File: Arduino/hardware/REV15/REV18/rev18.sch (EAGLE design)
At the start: 3 parts

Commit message: up to rev18 cleaned up
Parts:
- added IC1: DS1820, DS1820:DS1820
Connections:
- new net DQ: I2C_EXT.17
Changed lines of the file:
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@@
 <part name="GND1" library="SparkFun-Aesthetics" deviceset="GND" device=""/>
 <part name="U$4" library="SHT21" deviceset="SHT21" device=""/>
+<part name="IC1" library="DS1820" deviceset="DS1820" device=""/>
 </parts>
 <sheets>
@@
 <instance part="GND1" gate="1" x="256.54" y="180.34"/>
 <instance part="U$4" gate="G$1" x="241.3" y="182.88"/>
+<instance part="IC1" gate="G$1" x="157.48" y="185.42"/>
 </instances>
 <busses>
@@
 <label x="215.9" y="182.88" size="1.778" layer="95"/>
 <pinref part="U$4" gate="G$1" pin="V+"/>
+</segment>
+<segment>
+<wire x1="134.62" y1="187.96" x2="147.32" y2="187.96" width="0.1524" layer="91"/>
 </segment>
 </net>
@@
 <wire x1="254" y1="182.88" x2="256.54" y2="182.88" width="0.1524" layer="91"/>
 <pinref part="U$4" gate="G$1" pin="GND"/>
+</segment>
+<segment>
+<wire x1="157.48" y1="165.1" x2="157.48" y2="177.8" width="0.1524" layer="91"/>
 </segment>
 </net>
@@
 </segment>
 </net>
+<net name="DQ" class="0">
+<segment>
+<pinref part="I2C_EXT" gate="A" pin="17"/>
+<wire x1="157.48" y1="246.38" x2="165.1" y2="246.38" width="0.1524" layer="91"/>
+<label x="167.64" y="246.38" size="1.778" layer="95"/>
+</segment>
+<segment>
+<wire x1="167.64" y1="187.96" x2="175.26" y2="187.96" width="0.1524" layer="91"/>
+</segment>
+</net>

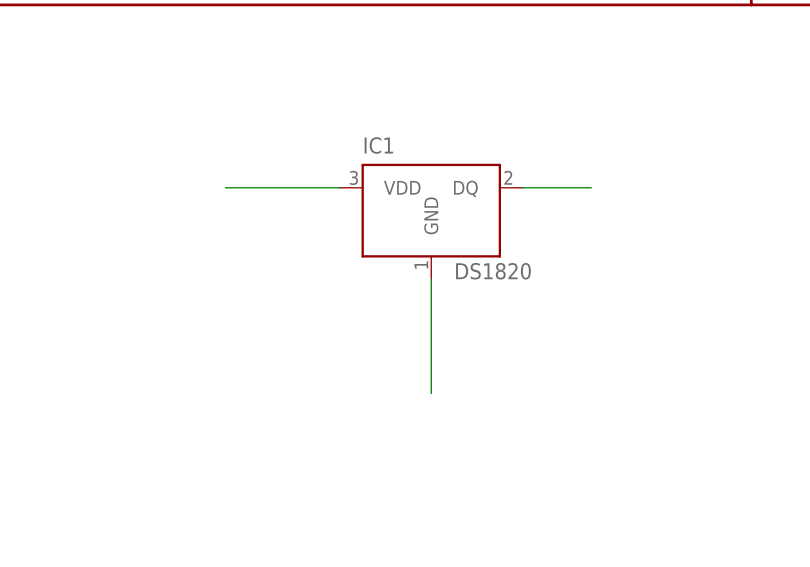
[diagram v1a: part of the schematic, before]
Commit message: up to rev18 DRC check and ground plane
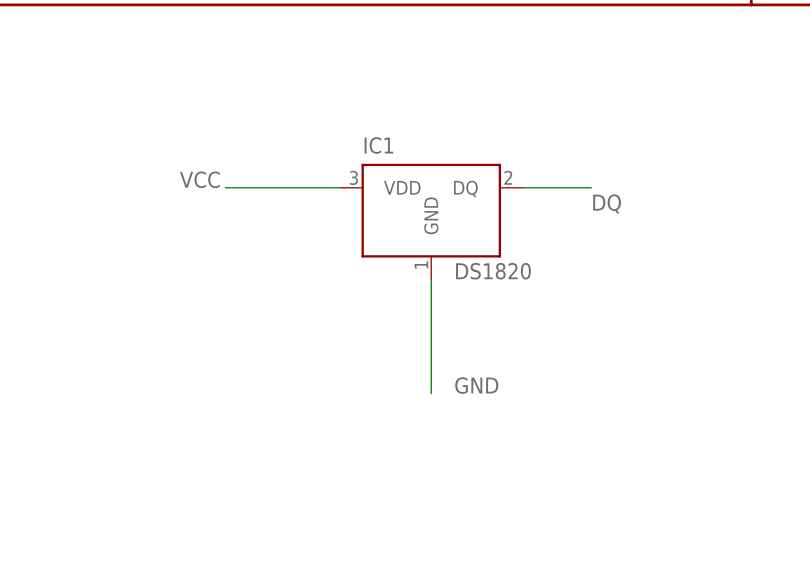
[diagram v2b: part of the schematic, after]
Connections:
- net DQ: now also IC1.DQ
- net GND: now also IC1.GND
- net VCC: now also IC1.VDD
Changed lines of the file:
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@@
 <segment>
 <wire x1="134.62" y1="187.96" x2="147.32" y2="187.96" width="0.1524" layer="91"/>
+<pinref part="IC1" gate="G$1" pin="VDD"/>
+<label x="129.54" y="187.96" size="1.778" layer="95"/>
 </segment>
 </net>
@@
 <segment>
 <wire x1="157.48" y1="165.1" x2="157.48" y2="177.8" width="0.1524" layer="91"/>
+<pinref part="IC1" gate="G$1" pin="GND"/>
+<label x="160.02" y="165.1" size="1.778" layer="95"/>
 </segment>
 </net>
@@
 <segment>
 <wire x1="167.64" y1="187.96" x2="175.26" y2="187.96" width="0.1524" layer="91"/>
+<pinref part="IC1" gate="G$1" pin="DQ"/>
+<label x="175.26" y="185.42" size="1.778" layer="95"/>
 </segment>
 </net>

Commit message: REV15-18 cleaned up, need sanity check
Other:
- note added: "Author(s) / Copyright (s): Bo Herrmannsen 2013--2016, Damon Hart-Davis 2013--2016, Mike Stirling 2013"
- note removed: "Author(s) / Copyright (s): Bo Herrmannsen 2013--2014, Damon Hart-Davis 2013--2014, Mike Stirling 2013"
- note removed: "OpenTRV Wireless TRV Controller"
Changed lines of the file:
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@@
 <text x="7.62" y="15.24" size="1.778" layer="91">software, hardware and materials distributed under this Licence</text>
 <text x="7.62" y="12.7" size="1.778" layer="91">is distributed on an "AS IS" BASIS, WITHOUT WARRANTIES OR CONDITIONS</text>
-<text x="7.62" y="2.54" size="1.778" layer="91">Author(s) / Copyright (s): Bo Herrmannsen 2013--2014, Damon Hart-Davis 2013--2014, Mike Stirling 2013</text>
-<text x="289.56" y="33.02" size="1.778" layer="91">OpenTRV Wireless TRV Controller</text>
+<text x="7.62" y="2.54" size="1.778" layer="91">Author(s) / Copyright (s): Bo Herrmannsen 2013--2016, Damon Hart-Davis 2013--2016, Mike Stirling 2013</text>
 <text x="7.62" y="10.16" size="1.778" layer="91"></text>
 <text x="7.62" y="10.16" size="1.778" layer="91">OF ANY KIND, either express or implied. See the Licence for the</text>
